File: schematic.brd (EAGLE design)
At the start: 98.3 x 134.6 mm, 32 parts, among them IC1 AD8015

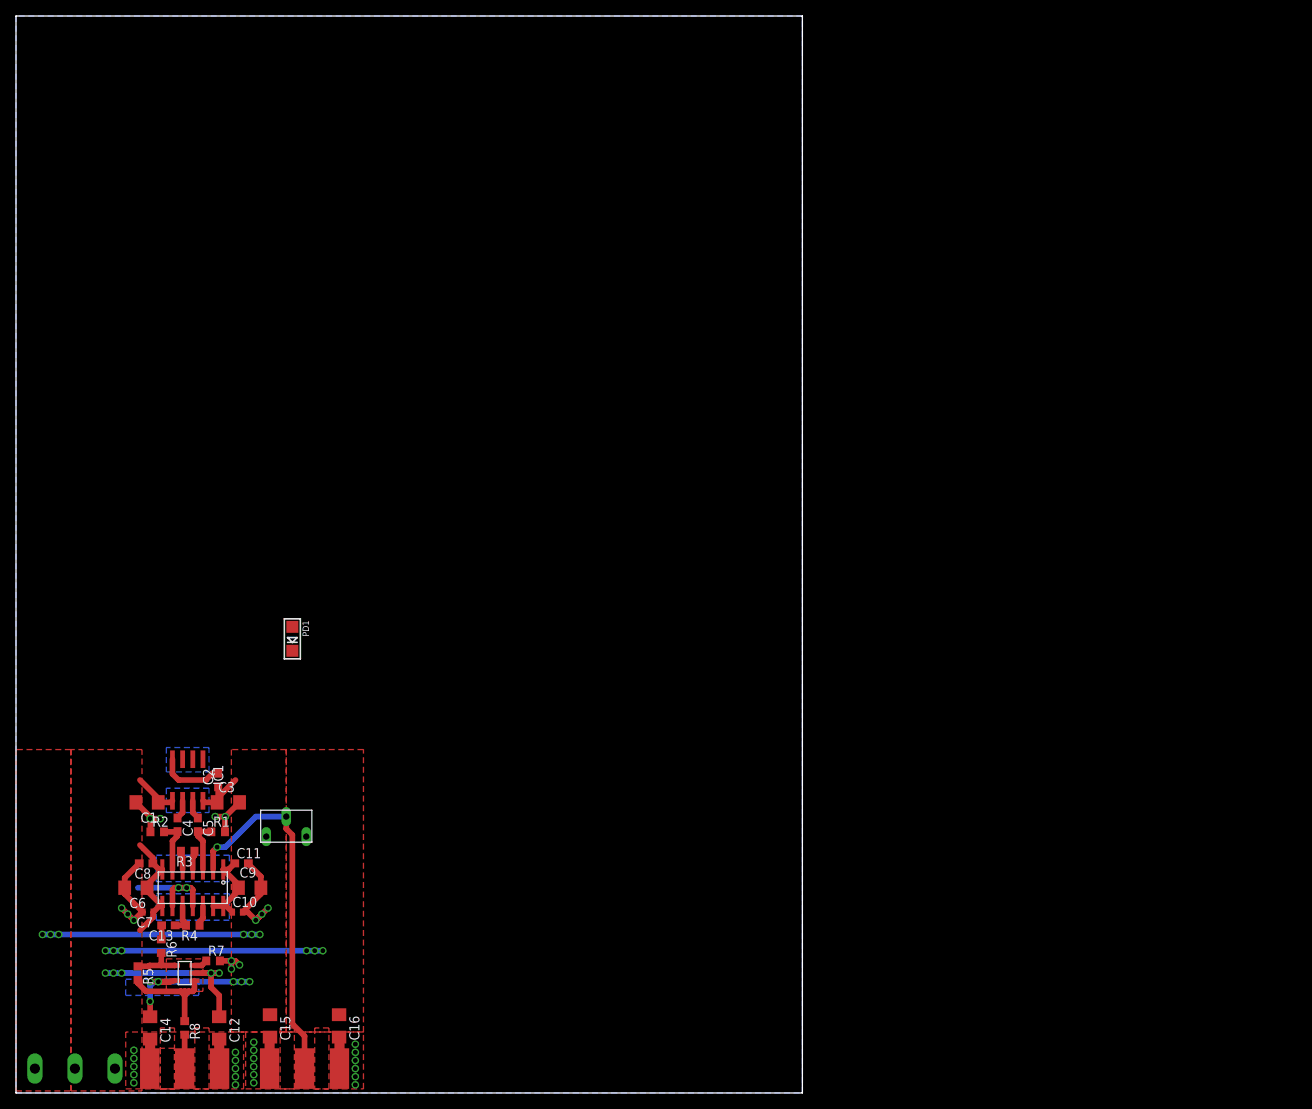
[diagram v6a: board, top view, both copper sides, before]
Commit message: Added second channel
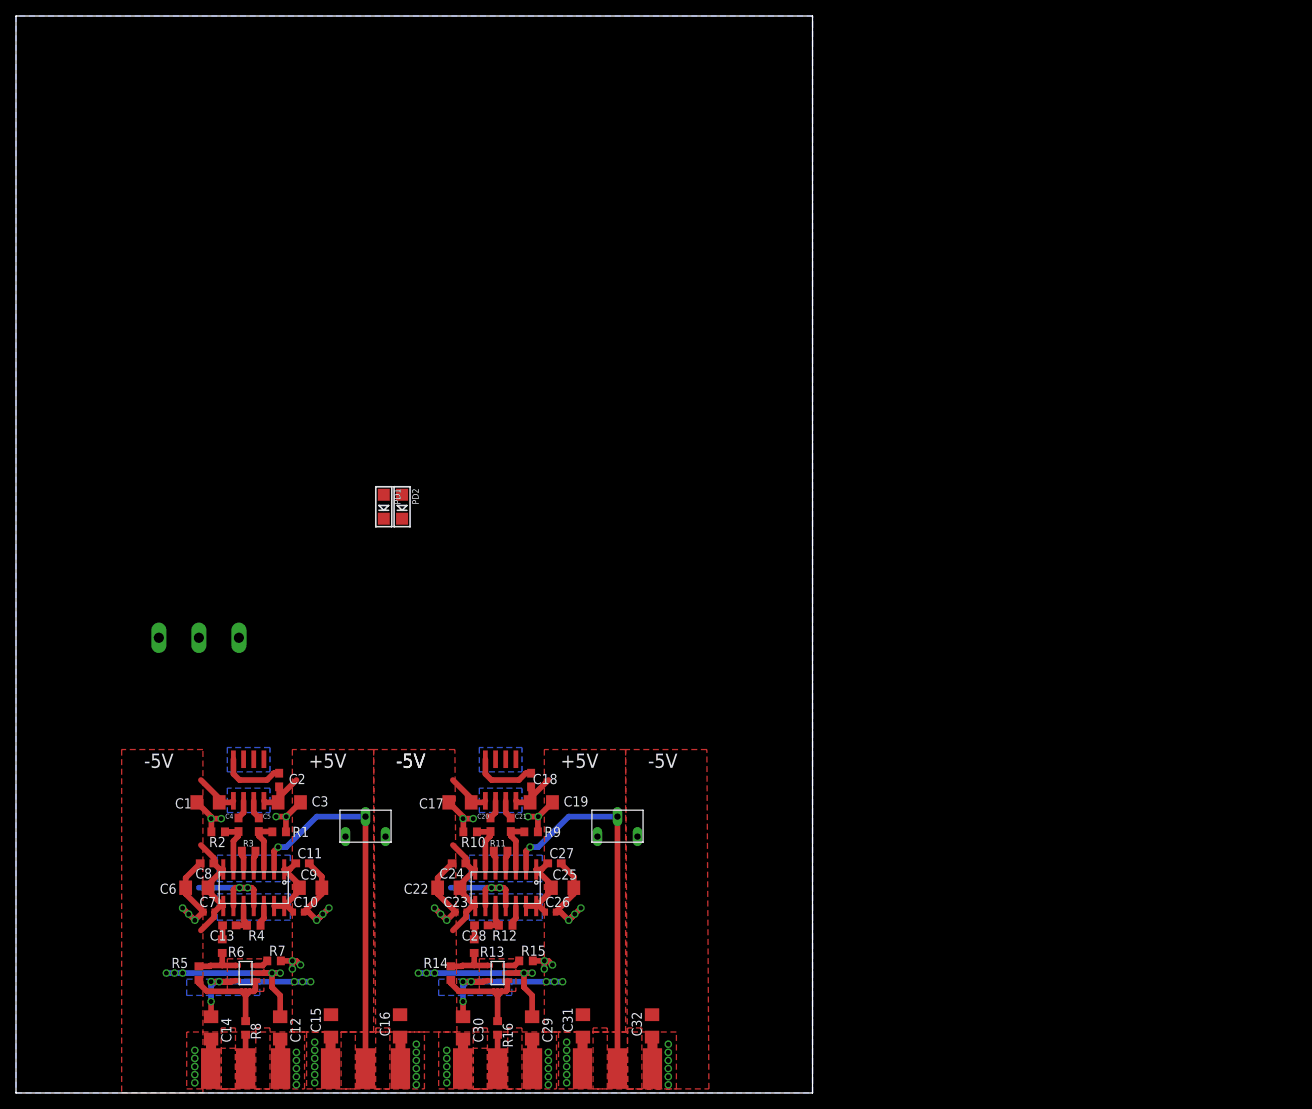
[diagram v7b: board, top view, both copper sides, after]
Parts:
- added C17, C19, C22, C25, C29, C30, C31, C32: 6.8uF, rcl:C1206
- added C18: .1uF, rcl:C0603
- added C20, C21, C28: 2.2uF, rcl:C0603
- added C23, C26: 0.1uF, rcl:C0402
- added C24, C27: 0.1uF, rcl:C0603
- added IC2: AD8015, analog-devices:SO8
- added PD2: (no value), microbuilder:CHIPLED_1206
- added R10, R16, R9: 50, rcl:R0603
- added R11: 100, rcl:R0603
- added R12: 1k, rcl:R0603
- added R13: 30, rcl:R0603
- added R14: 500, rcl:R0603
- added R15: 28, rcl:R0603
- added U$10, U$9: BNCCONN, 12-ChannelEMG:BNCPADS
- added U$11: LMH6624, 12-ChannelEMG:SOT-23
- added U$7: LMH6503, 12-ChannelEMG:SOIC14
- added U$8: PV37W, 12-ChannelEMG:PV37W
- moved U$3 56.0 mm to (22.9, 56.9), turned to 0 degrees
- moved PD1 20.1 mm to (46.0, 73.3)
- moved U$2 9.91 mm to (43.7, 34.5)
- moved C12 7.62 mm to (33.0, 8.13)
- moved U$4 7.62 mm to (43.7, 3.05)
- moved C1 7.62 mm to (24.0, 36.3)
- moved C11 7.62 mm to (35.8, 28.7)
- moved C13 7.62 mm to (26.7, 21.0)
- moved C14 7.62 mm to (24.4, 8.13)
- moved C2 7.62 mm to (32.9, 39.1)
- moved C5 7.62 mm to (30.4, 33.5)
- moved C6 7.62 mm to (22.6, 25.7)
- moved C8 7.62 mm to (23.9, 28.7)
- moved R1 7.62 mm to (32.9, 32.6)
- moved R2 7.62 mm to (25.3, 32.6)
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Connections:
- new net N$25: C18.2, IC2.4
- new net N$26: IC2.2, PD2.C
- new net N$27: C21.1, IC2.7
- new net N$28: C20.1, IC2.6
- new net N$29: C20.2, R10.2, U$7.6
- new net N$30: C21.2, R9.1, U$7.3
- new net N$31: R11.1, U$7.4
- new net N$32: R11.2, U$7.5
- new net N$33: R12.1, U$7.12
- new net N$34: C28.1, R12.2, U$7.10
- new net N$35: C28.2, R13.1
- new net N$36: U$7.2, U$8.2, U$9.2
- new net N$37: R13.2, R14.1, U$11.4
- new net N$38: R15.1, U$11.3
- new net N$39: R14.2, R16.1, U$11.1
- new net N$40: R16.2, U$10.2
- net +5V: now also C18.1, C19.1, C25.1, C26.1, C27.1, C30.1, C31.1, IC2.8, U$11.5, U$7.1, U$7.13, U$7.14, U$8.1
- net -5V: now also C17.1, C22.1, C23.1, C24.1, C29.1, C32.1, IC2.5, PD2.A, U$11.2, U$7.7, U$7.8, U$8.3
- net GND: now also C17.2, C19.2, C22.2, C23.2, C24.2, C25.2, C26.2, C27.2, C29.2, C30.2, C31.2, C32.2, R10.1, R15.2, R9.2, U$10.1, U$10.3, U$7.11, U$7.9, U$9.1, U$9.3
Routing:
- net GND: track 69.0 -> 137.9 mm, vias 37 -> 74
- net N$36: track 0.00 -> 46.7 mm, vias 0 -> 1
- net -5V: track 72.0 -> 89.7 mm, vias 11 -> 10
- net N$39: track 0.00 -> 14.3 mm
- net +5V: track 67.5 -> 80.6 mm
- net N$25: track 0.00 -> 8.22 mm
- net N$30: track 0.00 -> 6.71 mm
- net N$29: track 0.00 -> 6.65 mm
- net N$37: track 0.00 -> 6.23 mm
- net N$40: track 0.00 -> 4.23 mm
- net N$34: track 0.00 -> 3.93 mm
- net N$31: track 0.00 -> 2.88 mm
- net N$33: track 0.00 -> 2.59 mm
- net N$28: track 0.00 -> 2.40 mm
- net N$27: track 0.00 -> 2.40 mm
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- added copper zone on layer 1, net N$41
- added copper zone on layer 16, net N$41
- added copper zone on layer 1, net N$42
- added copper zone on layer 1, net N$43
- added copper zone on layer 16, net N$43
- added copper zone on layer 1, net N$44
- added copper zone on layer 1, net N$45
- added copper zone on layer 1, net N$46
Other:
- board size 98.3 x 134.6 mm -> 99.6 x 134.6 mm

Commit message: Added third channel
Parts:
- added C33, C35, C38, C41, C45, C46, C47, C48: 6.8uF, rcl:C1206
- added C34: .1uF, rcl:C0603
- added C36, C37, C44: 2.2uF, rcl:C0603
- added C39, C42: 0.1uF, rcl:C0402
- added C40, C43: 0.1uF, rcl:C0603
- added IC3: AD8015, analog-devices:SO8
- added PD3: (no value), microbuilder:CHIPLED_1206
- added R17, R18, R24: 50, rcl:R0603
- added R19: 100, rcl:R0603
- added R20: 1k, rcl:R0603
- added R21: 30, rcl:R0603
- added R22: 500, rcl:R0603
- added R23: 28, rcl:R0603
- added U$12: LMH6503, 12-ChannelEMG:SOIC14
- added U$13: PV37W, 12-ChannelEMG:PV37W
- added U$14, U$15: BNCCONN, 12-ChannelEMG:BNCPADS
- added U$16: LMH6624, 12-ChannelEMG:SOT-23
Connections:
- new net N$47: C34.2, IC3.4
- new net N$48: IC3.2, PD3.C
- new net N$49: C37.1, IC3.7
- new net N$50: C36.1, IC3.6
- new net N$51: C36.2, R18.2, U$12.6
- new net N$52: C37.2, R17.1, U$12.3
- new net N$53: R19.1, U$12.4
- new net N$54: R19.2, U$12.5
- new net N$55: R20.1, U$12.12
- new net N$56: C44.1, R20.2, U$12.10
- new net N$57: C44.2, R21.1
- new net N$58: U$12.2, U$13.2, U$14.2
- new net N$59: R21.2, R22.1, U$16.4
- new net N$60: R23.1, U$16.3
- new net N$61: R22.2, R24.1, U$16.1
- new net N$62: R24.2, U$15.2
- net +5V: now also C34.1, C35.1, C41.1, C42.1, C43.1, C46.1, C47.1, IC3.8, U$12.1, U$12.13, U$12.14, U$13.1, U$16.5
- net -5V: now also C33.1, C38.1, C39.1, C40.1, C45.1, C48.1, IC3.5, PD3.A, U$12.7, U$12.8, U$13.3, U$16.2
- net GND: now also C33.2, C35.2, C38.2, C39.2, C40.2, C41.2, C42.2, C43.2, C45.2, C46.2, C47.2, C48.2, R17.2, R18.1, R23.2, U$12.11, U$12.9, U$14.1, U$14.3, U$15.1, U$15.3
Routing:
- net GND: track 137.9 -> 206.9 mm, vias 74 -> 117
- net N$58: track 0.00 -> 46.7 mm, vias 0 -> 1
- net -5V: track 89.7 -> 134.5 mm, vias 10 -> 15
- net +5V: track 80.6 -> 120.9 mm, vias 12 -> 18
- net N$61: track 0.00 -> 14.3 mm
- net N$47: track 0.00 -> 8.22 mm
- net N$52: track 0.00 -> 6.71 mm
- net N$51: track 0.00 -> 6.65 mm
- net N$59: track 0.00 -> 6.23 mm
- net N$62: track 0.00 -> 4.23 mm
- net N$56: track 0.00 -> 3.93 mm
- net N$53: track 0.00 -> 2.88 mm
- net N$55: track 0.00 -> 2.59 mm
- net N$50: track 0.00 -> 2.40 mm
- net N$49: track 0.00 -> 2.40 mm
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- added copper zone on layer 1, net N$63
- added copper zone on layer 16, net N$63
- added copper zone on layer 1, net N$64
- added copper zone on layer 1, net N$65
- added copper zone on layer 16, net N$65
- added copper zone on layer 1, net N$66
- added copper zone on layer 1, net N$67
- added copper zone on layer 1, net N$68
